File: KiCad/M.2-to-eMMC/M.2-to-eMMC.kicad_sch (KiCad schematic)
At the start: 1 part, among them J1 M.2 E Key Connector

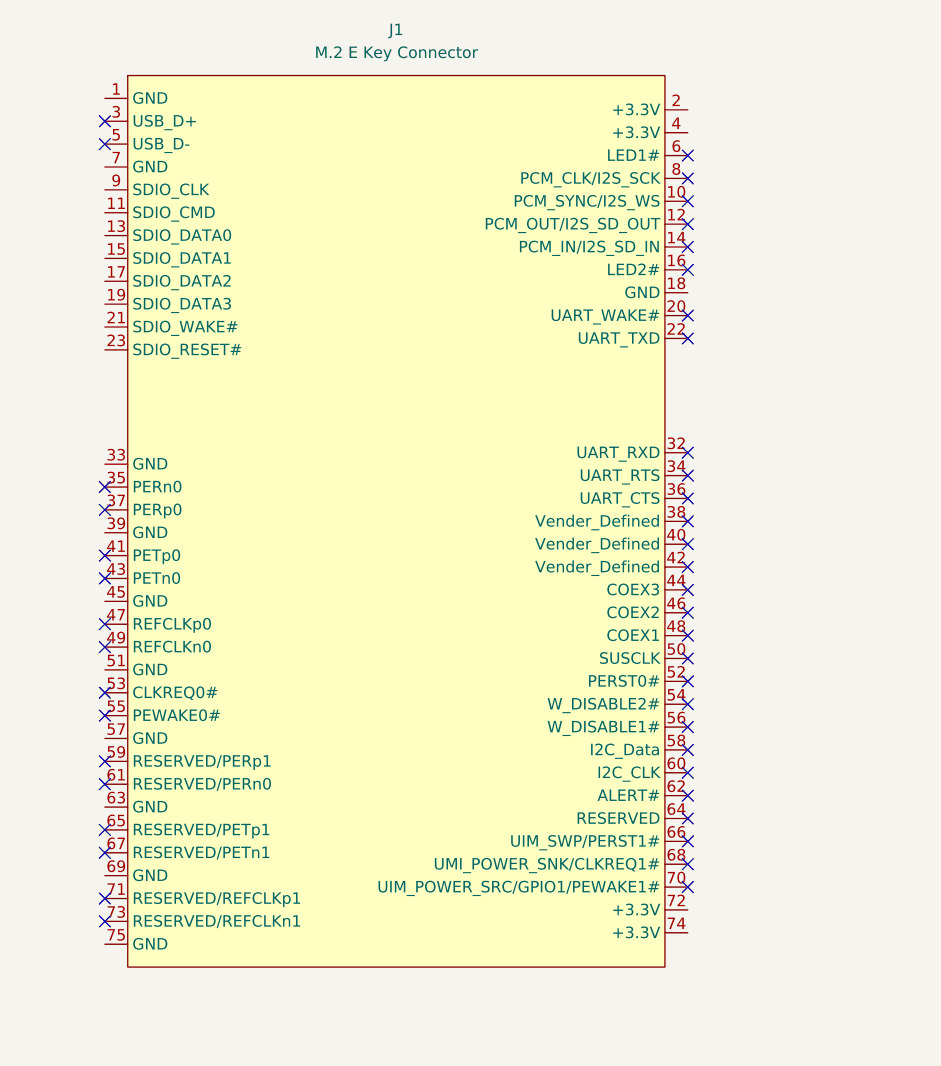
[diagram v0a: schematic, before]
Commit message: Update M.2-to-eMMC.kicad_sch
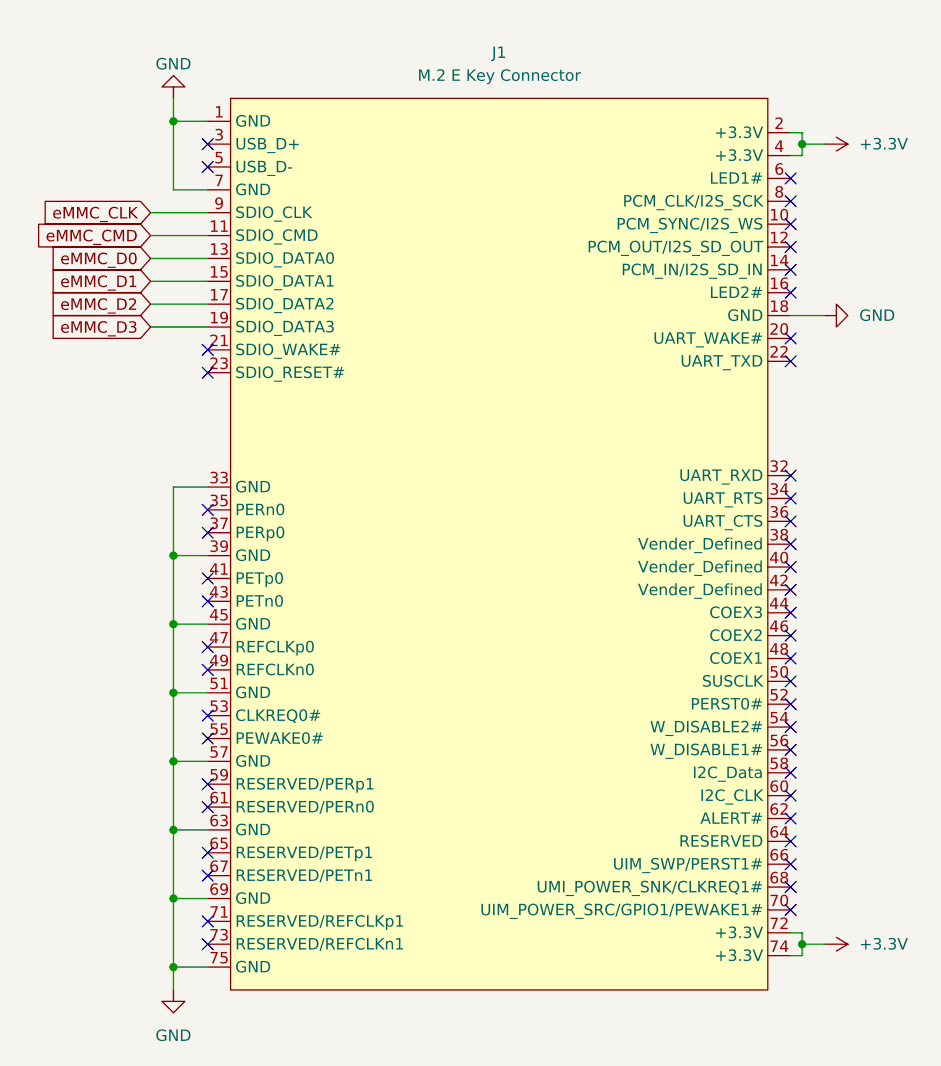
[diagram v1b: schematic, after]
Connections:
- net GND: now reaches J1.1 (GND)
- net GND: now also J1.18 (GND), J1.33 (GND), J1.39 (GND), J1.45 (GND), J1.51 (GND), J1.57 (GND), J1.63 (GND), J1.69 (GND), J1.7 (GND), J1.75 (GND)
- net eMMC_CMD: now reaches J1.11 (SDIO_CMD)
- net eMMC_D0: now reaches J1.13 (SDIO_DATA0)
- net eMMC_D1: now reaches J1.15 (SDIO_DATA1)
- net eMMC_D2: now reaches J1.17 (SDIO_DATA2)
- net eMMC_D3: now reaches J1.19 (SDIO_DATA3)
- net +3.3V: now reaches J1.2 (+3.3V)
- net +3.3V: now also J1.4 (+3.3V), J1.72 (+3.3V), J1.74 (+3.3V)
- net eMMC_CLK: now reaches J1.9 (SDIO_CLK)
- no-connect marks 44 -> 46
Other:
- moved on the sheet: J1
